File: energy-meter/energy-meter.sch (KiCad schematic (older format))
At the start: 28 parts, among them J1 Screw_Terminal_01x04, J2 Conn_01x03, K1 G5RL-U1A-E, P1 PineNut, T1 AP-2500, T2 BV 202 0154, U1 L9110S, U9 GD32VF103

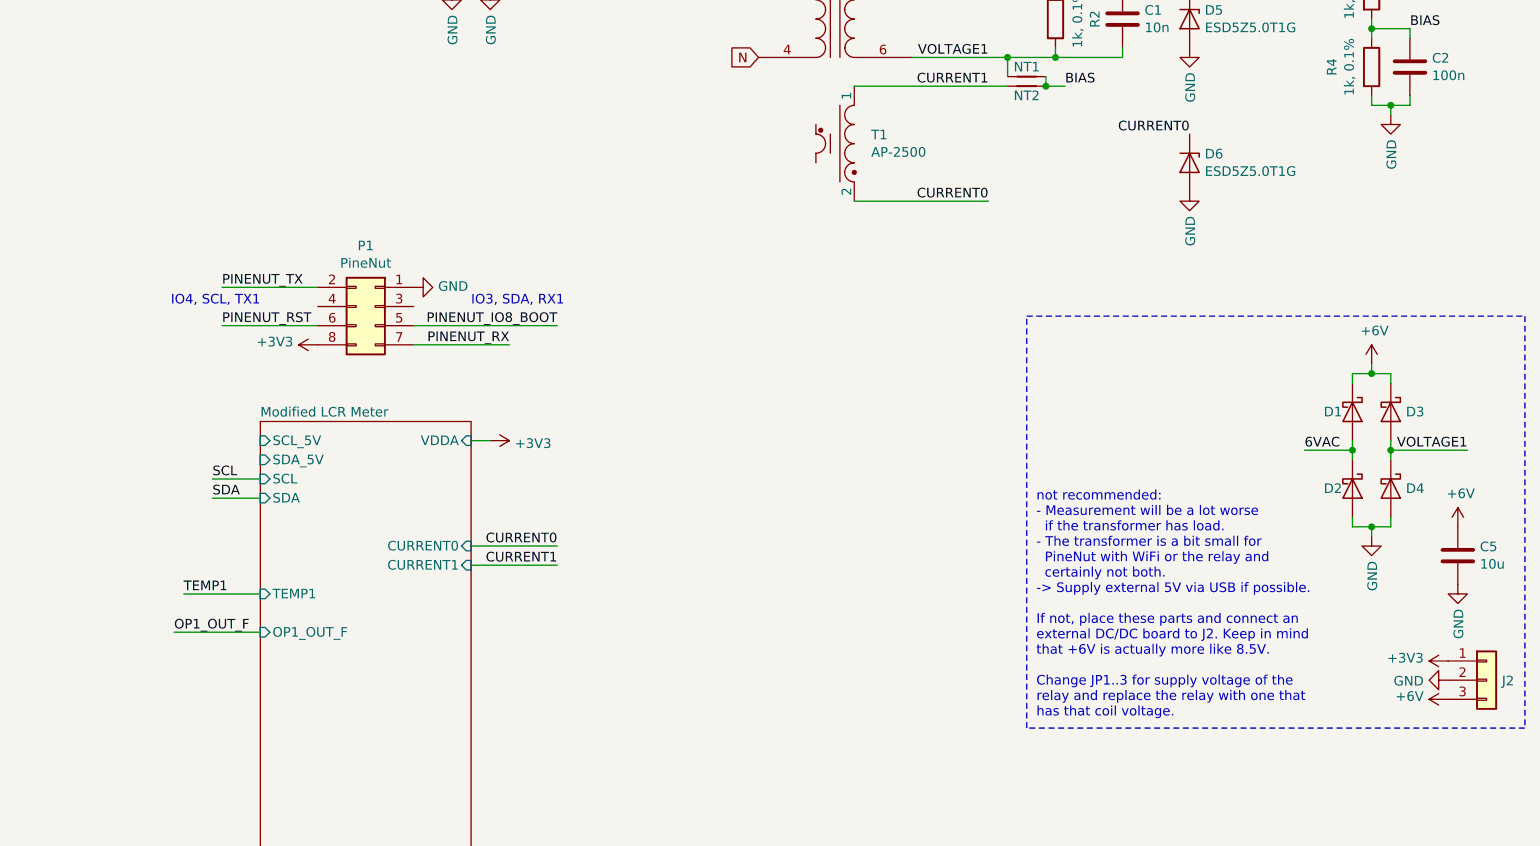
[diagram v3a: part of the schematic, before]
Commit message: DRC, add header for I2C
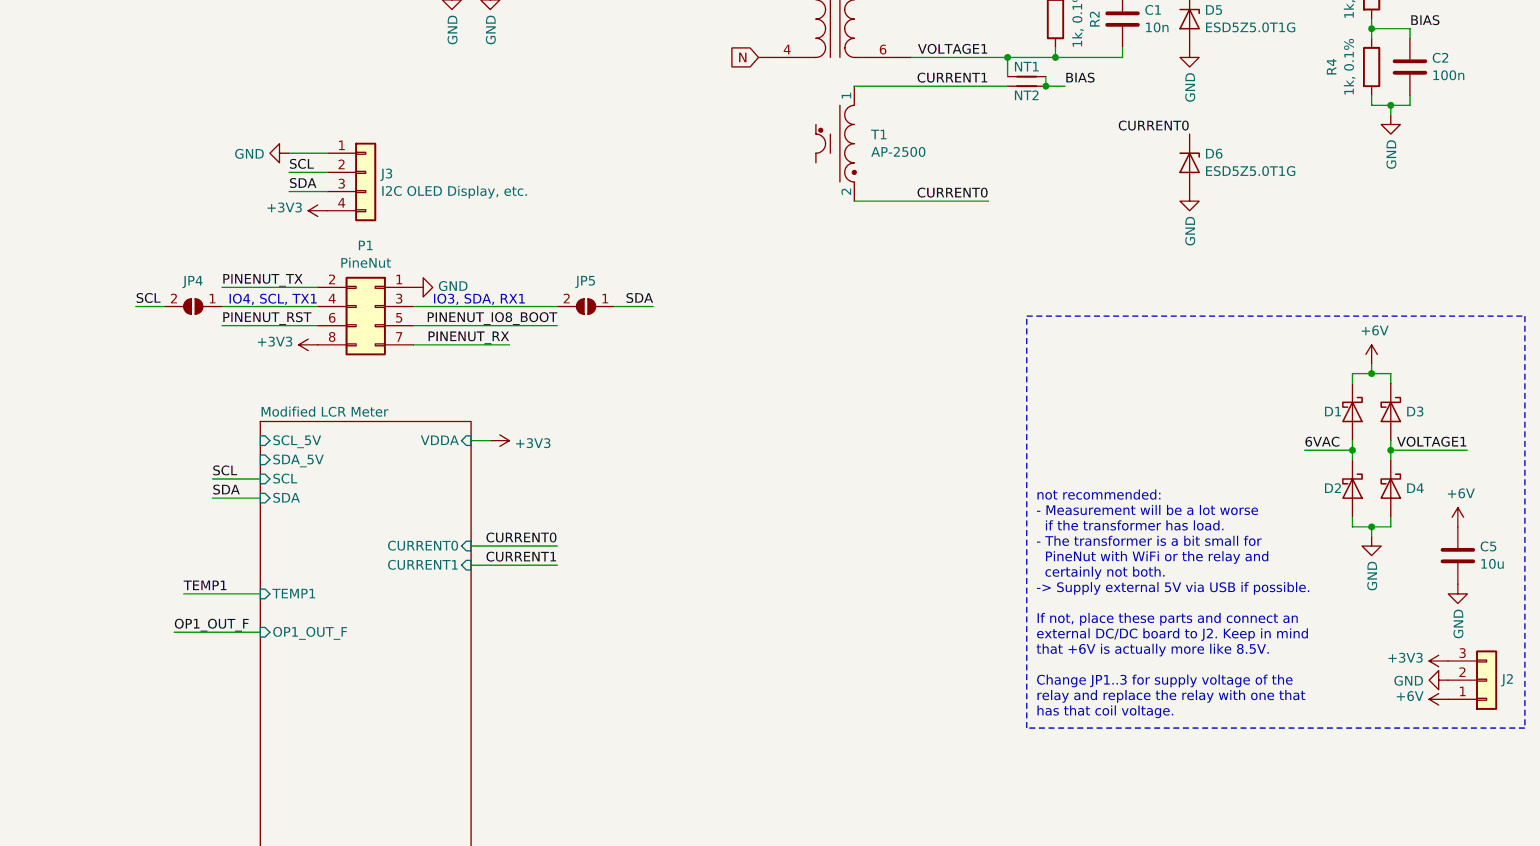
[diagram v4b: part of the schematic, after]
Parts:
- added J3: I2C OLED Display, etc., Connector_PinHeader_2.54mm:PinHeader_1x04_P2.54mm_Horizontal, symbol Connector_Generic:Conn_01x04
- added JP4, JP5: SolderJumper_2_Open, Jumper:SolderJumper-2_P1.3mm_Open_RoundedPad1.0x1.5mm, symbol Jumper:SolderJumper_2_Open
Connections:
- net +3V3: now also J2.3 (Pin_3), J3.4 (Pin_4); no longer J2.1 (Pin_1)
- net +6V: now also J2.1 (Pin_1); no longer J2.3 (Pin_3)
- net GND: now also J3.1 (Pin_1)
- net SCL: now also J3.2 (Pin_2), JP4.2 (B)
- net SDA: now also J3.3 (Pin_3), JP5.1 (A)
- net at P1.3 (Pin_3): now also JP5.2 (B)
- net at P1.4 (Pin_4): now also JP4.1 (A)
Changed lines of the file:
@@
 	0    -1   -1   0
 $EndComp
-Text Notes 5600 4250 0    50   ~ 0
+Text Notes 5400 4250 0    50   ~ 0
 IO3, SDA, RX1
-Text Notes 4500 4250 2    50   ~ 0
+Text Notes 4800 4250 2    50   ~ 0
 IO4, SCL, TX1
 $Comp
@@
 F 3 "~" H 10900 6200 50  0001 C CNN
 	1    10900 6200
-	1    0    0    -1
+	1    0    0    1
 $EndComp
 $Comp
@@
 Text Label 9350 3350 2    50   ~ 0
 CURRENT0
+Text Label 3850 4250 0    50   ~ 0
+SCL
+Wire Wire Line
+	4300 4250 4800 4250
+$Comp
+L Jumper:SolderJumper_2_Open JP4
+U 1 1 60C77BF5
+P 4150 4250
+F 0 "JP4" H 4150 4117 50  0000 C CNN
+F 1 "SolderJumper_2_Open" H 4150 4364 50  0001 C CNN
+F 2 "Jumper:SolderJumper-2_P1.3mm_Open_RoundedPad1.0x1.5mm" H 4150 4250 50  0001 C CNN
+F 3 "~" H 4150 4250 50  0001 C CNN
+	1    4150 4250
+	-1   0    0    1
+$EndComp
+Wire Wire Line
+	3850 4250 4000 4250
+Wire Wire Line
+	5300 4250 6050 4250
+$Comp
+L Jumper:SolderJumper_2_Open JP5
+U 1 1 60C8116D
+P 6200 4250
+F 0 "JP5" H 6200 4117 50  0000 C CNN
+F 1 "SolderJumper_2_Open" H 6200 4364 50  0001 C CNN
+F 2 "Jumper:SolderJumper-2_P1.3mm_Open_RoundedPad1.0x1.5mm" H 6200 4250 50  0001 C CNN
+F 3 "~" H 6200 4250 50  0001 C CNN
+	1    6200 4250
+	-1   0    0    1
+$EndComp
+Text Label 6550 4250 2    50   ~ 0
+SDA
+Wire Wire Line
+	6550 4250 6350 4250
+$Comp
+L Connector_Generic:Conn_01x04 J3
+U 1 1 60C9802A
+P 5050 3550
+F 0 "J3" H 5130 3542 50  0000 L CNN
+F 1 "I2C OLED Display, etc." H 5130 3451 50  0000 L CNN
+F 2 "Connector_PinHeader_2.54mm:PinHeader_1x04_P2.54mm_Horizontal" H 5050 3550 50  0001 C CNN
+F 3 "~" H 5050 3550 50  0001 C CNN
+	1    5050 3550
+	1    0    0    -1
+$EndComp
+$Comp
+L power:GND #PWR0136
+U 1 1 60C999E8
+P 4650 3450
+F 0 "#PWR0136" H 4650 3200 50  0001 C CNN
+F 1 "GND" V 4655 3322 50  0000 R CNN
+F 2 "" H 4650 3450 50  0001 C CNN
+F 3 "" H 4650 3450 50  0001 C CNN
+	1    4650 3450
+	0    1    1    0
+$EndComp
+Text Label 4650 3550 0    50   ~ 0
+SCL
+Wire Wire Line
+	4650 3550 4850 3550
+Text Label 4650 3650 0    50   ~ 0
+SDA
+Wire Wire Line
+	4650 3650 4850 3650
+$Comp
+L power:+3V3 #PWR?
+U 1 1 60CA251B
+P 4850 3750
+AR Path="/607B74C2/60CA251B" Ref="#PWR?"  Part="1"
+AR Path="/60CA251B" Ref="#PWR0137"  Part="1"
+F 0 "#PWR0137" H 4850 3600 50  0001 C CNN
+F 1 "+3V3" V 4865 3878 50  0000 L CNN
+F 2 "" H 4850 3750 50  0001 C CNN
+F 3 "" H 4850 3750 50  0001 C CNN
+	1    4850 3750
+	0    -1   -1   0
+$EndComp
+Wire Wire Line
+	4650 3450 4850 3450
 $EndSCHEMATC

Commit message: add alternative relay
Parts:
- added K2: DNP / HF3FF/005-1HST, energy-meter:Relay_HF3FF_005, symbol Relay:DIPxx-1Axx-11x
- added T3: DNP / AP-2500, energy-meter:AP-2500, symbol energy-meter:AP-2500
- added TP?: TestPoint, TestPoint:TestPoint_THTPad_D3.0mm_Drill1.5mm, symbol Connector:TestPoint
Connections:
- net labels added: coil+, coil-
- wire segments 114 -> 125
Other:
- note added: "alternative relay:\ncheap but not bistable"
- note added: "connect with wire"
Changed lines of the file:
@@
 Wire Wire Line
 	4650 3450 4850 3450
+$Comp
+L Relay:DIPxx-1Axx-11x K2
+U 1 1 60CDDACF
+P 9700 1200
+F 0 "K2" H 10030 1246 50  0000 L CNN
+F 1 "DNP / HF3FF/005-1HST" H 10030 1155 50  0000 L CNN
+F 2 "energy-meter:Relay_HF3FF_005" H 10050 1150 50  0001 L CNN
+F 3 "https://standexelectronics.com/wp-content/uploads/datasheet_reed_relay_DIP.pdf" H 9700 1200 50  0001 C CNN
+F 4 "https://www.tme.eu/de/details/hf3ff_005-1hst/elektromagnetische-mini-relais/hongfa-relay/" H 9700 1200 50  0001 C CNN "TME"
+	1    9700 1200
+	1    0    0    -1
+$EndComp
+Text GLabel 9950 850  2    50   Input ~ 0
+L_OUT
+Wire Wire Line
+	9950 850  9900 850
+Wire Wire Line
+	9900 850  9900 900
+Text GLabel 10350 1550 2    50   Input ~ 0
+L_IN
+Wire Wire Line
+	9900 1550 9900 1500
+Text Notes 9550 750  0    50   ~ 0
+alternative relay:\ncheap but not bistable
+Text Label 6850 2200 0    50   ~ 0
+coil+
+Text Label 6850 1500 0    50   ~ 0
+coil-
+Text Label 9100 850  0    50   ~ 0
+coil-
+Text Label 9100 1550 0    50   ~ 0
+coil+
+Wire Wire Line
+	9100 1550 9500 1550
+Wire Wire Line
+	9500 1550 9500 1500
+Wire Wire Line
+	9100 850  9500 850
+Wire Wire Line
+	9500 850  9500 900
+Text Notes 10050 1700 0    50   ~ 0
+connect with wire
+$Comp
+L energy-meter:AP-2500 T3
+U 1 1 60CFE5A9
+P 7100 3400
+F 0 "T3" V 7050 3250 50  0000 L CNN
+F 1 "DNP / AP-2500" V 7150 2750 50  0000 L CNN
+F 2 "energy-meter:AP-2500" H 7100 3400 50  0001 C CNN
+F 3 "https://www.coilcraft.com/pdfs/cst.pdf" H 7100 3400 50  0001 C CNN
+F 4 "https://www.tme.eu/de/details/ap-2500/stromwandler/talema/" V 7100 3400 50  0001 C CNN "TME"
+	1    7100 3400
+	0    1    1    0
+$EndComp
+Wire Wire Line
+	7300 3100 7600 3100
+Connection ~ 7600 3100
+Wire Wire Line
+	7600 3700 7300 3700
+Connection ~ 7600 3700
+$Comp
+L Connector:TestPoint TP?
+U 1 1 60D46B3F
+P 9900 1550
+F 0 "TP?" H 9950 1800 50  0000 R CNN
+F 1 "TestPoint" H 9958 1577 50  0001 L CNN
+F 2 "TestPoint:TestPoint_THTPad_D3.0mm_Drill1.5mm" H 10100 1550 50  0001 C CNN
+F 3 "~" H 10100 1550 50  0001 C CNN
+	1    9900 1550
+	-1   0    0    1
+$EndComp
+Connection ~ 9900 1550
+Wire Wire Line
+	10350 1550 10200 1550
+Wire Wire Line
+	9900 1550 10100 1550
 $EndSCHEMATC

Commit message: add optional internal load resistor
This may be useful for calibration and tests.
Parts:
- added R5: 39kOhm, 2W, 1%, Resistor_SMD:R_2512_6332Metric_Pad1.52x3.35mm_HandSolder, symbol Device:R
- added TP2, TP3, TP4, TP5: TestPoint, TestPoint:TestPoint_THTPad_D3.0mm_Drill1.5mm, symbol Connector:TestPoint
- gave numbers to parts that had none: 1
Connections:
- wire segments 125 -> 133
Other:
- note added: "alternative use of the 2nd relay:\n- cut L_OUT around TP3\n- TP3 -> through T3 -> TP5\n- N -> TP4\n- L_OUT to external load, as usual\n=> K2 enables internal load"
- moved on the sheet: C2, R3, R4, TP1
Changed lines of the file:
@@
 P 7750 900
 F 0 "J1" H 7830 892 50  0000 L CNN
-F 1 "Screw_Terminal_01x04" H 7830 801 50  0000 L CNN
+F 1 "Screw_Terminal_01x04" H 7830 801 50  0001 L CNN
 F 2 "energy-meter:DG35C-B-04P-13-200AH" H 7750 900 50  0001 C CNN
 F 3 "~" H 7750 900 50  0001 C CNN
@@
 U 1 1 60929B00
 P 7500 2750
-F 0 "T2" H 7500 3131 50  0000 C CNN
+F 0 "T2" H 7300 2750 50  0000 C CNN
 F 1 "BV 202 0154" H 7500 3040 50  0000 C CNN
 F 2 "energy-meter:BV202" H 7500 2750 50  0001 C CNN
@@
 Wire Wire Line
 	6050 5600 5600 5600
-Text Label 8700 2550 0    50   ~ 0
+Text Label 9050 2550 0    50   ~ 0
 VOLTAGE0
 Text Label 8300 2950 2    50   ~ 0
@@
 L Device:R R?
 U 1 1 60A38A5B
-P 10300 3000
+P 10500 3300
 AR Path="/602A3FC4/60A38A5B" Ref="R?"  Part="1"
 AR Path="/60514CC5/60A38A5B" Ref="R?"  Part="1"
 AR Path="/607B74C2/60A38A5B" Ref="R?"  Part="1"
 AR Path="/60A38A5B" Ref="R4"  Part="1"
-F 0 "R4" V 10093 3000 50  0000 C CNN
-F 1 "1k, 0.1%" V 10184 3000 50  0000 C CNN
-F 2 "Resistor_SMD:R_0603_1608Metric_Pad1.05x0.95mm_HandSolder" V 10230 3000 50  0001 C CNN
-F 3 "~" H 10300 3000 50  0001 C CNN
-	1    10300 3000
+F 0 "R4" V 10293 3300 50  0000 C CNN
+F 1 "1k, 0.1%" V 10384 3300 50  0000 C CNN
+F 2 "Resistor_SMD:R_0603_1608Metric_Pad1.05x0.95mm_HandSolder" V 10430 3300 50  0001 C CNN
+F 3 "~" H 10500 3300 50  0001 C CNN
+	1    10500 3300
 	1    0    0    -1
 $EndComp
@@
 L Device:C C?
 U 1 1 60A38A61
-P 10500 3000
+P 10700 3300
 AR Path="/602A2F7F/60A38A61" Ref="C?"  Part="1"
 AR Path="/602A3FC4/60A38A61" Ref="C?"  Part="1"
@@
 AR Path="/607B74C2/60A38A61" Ref="C?"  Part="1"
 AR Path="/60A38A61" Ref="C2"  Part="1"
-F 0 "C2" H 10615 3046 50  0000 L CNN
-F 1 "100n" H 10615 2955 50  0000 L CNN
-F 2 "Capacitor_SMD:C_0603_1608Metric_Pad1.05x0.95mm_HandSolder" H 10538 2850 50  0001 C CNN
-F 3 "~" H 10500 3000 50  0001 C CNN
-	1    10500 3000
+F 0 "C2" H 10815 3346 50  0000 L CNN
+F 1 "100n" H 10815 3255 50  0000 L CNN
+F 2 "Capacitor_SMD:C_0603_1608Metric_Pad1.05x0.95mm_HandSolder" H 10738 3150 50  0001 C CNN
+F 3 "~" H 10700 3300 50  0001 C CNN
+	1    10700 3300
 	1    0    0    -1
 $EndComp
@@
 L power:+3V3 #PWR?
 U 1 1 60A3967A
-P 10300 2400
+P 10500 2700
 AR Path="/607B74C2/60A3967A" Ref="#PWR?"  Part="1"
 AR Path="/60A3967A" Ref="#PWR0106"  Part="1"
-F 0 "#PWR0106" H 10300 2250 50  0001 C CNN
-F 1 "+3V3" V 10315 2528 50  0000 L CNN
-F 2 "" H 10300 2400 50  0001 C CNN
-F 3 "" H 10300 2400 50  0001 C CNN
-	1    10300 2400
+F 0 "#PWR0106" H 10500 2550 50  0001 C CNN
+F 1 "+3V3" V 10515 2828 50  0000 L CNN
+F 2 "" H 10500 2700 50  0001 C CNN
+F 3 "" H 10500 2700 50  0001 C CNN
+	1    10500 2700
 	1    0    0    -1
 $EndComp
@@
 L Device:R R?
 U 1 1 60A3A4C3
-P 10300 2600
+P 10500 2900
 AR Path="/602A3FC4/60A3A4C3" Ref="R?"  Part="1"
 AR Path="/60514CC5/60A3A4C3" Ref="R?"  Part="1"
 AR Path="/607B74C2/60A3A4C3" Ref="R?"  Part="1"
 AR Path="/60A3A4C3" Ref="R3"  Part="1"
-F 0 "R3" V 10093 2600 50  0000 C CNN
-F 1 "1k, 0.1%" V 10184 2600 50  0000 C CNN
-F 2 "Resistor_SMD:R_0603_1608Metric_Pad1.05x0.95mm_HandSolder" V 10230 2600 50  0001 C CNN
-F 3 "~" H 10300 2600 50  0001 C CNN
-	1    10300 2600
-	1    0    0    -1
-$EndComp
-Wire Wire Line
-	10500 3150 10500 3200
-Wire Wire Line
-	10500 3200 10400 3200
-Wire Wire Line
-	10400 3200 10400 3250
-Wire Wire Line
-	10400 3200 10300 3200
-Wire Wire Line
-	10300 3200 10300 3150
-Connection ~ 10400 3200
-Wire Wire Line
-	10300 2850 10300 2800
-Wire Wire Line
-	10300 2800 10500 2800
-Wire Wire Line
-	10500 2800 10500 2850
-Connection ~ 10300 2800
-Wire Wire Line
-	10300 2800 10300 2750
-Wire Wire Line
-	10300 2450 10300 2400
+F 0 "R3" V 10293 2900 50  0000 C CNN
+F 1 "1k, 0.1%" V 10384 2900 50  0000 C CNN
+F 2 "Resistor_SMD:R_0603_1608Metric_Pad1.05x0.95mm_HandSolder" V 10430 2900 50  0001 C CNN
+F 3 "~" H 10500 2900 50  0001 C CNN
+	1    10500 2900
+	1    0    0    -1
+$EndComp
+Wire Wire Line
+	10700 3450 10700 3500
+Wire Wire Line
+	10700 3500 10600 3500
+Wire Wire Line
+	10600 3500 10600 3550
+Wire Wire Line
+	10600 3500 10500 3500
+Wire Wire Line
+	10500 3500 10500 3450
+Connection ~ 10600 3500
+Wire Wire Line
+	10500 3150 10500 3100
+Wire Wire Line
+	10500 3100 10700 3100
+Wire Wire Line
+	10700 3100 10700 3150
+Connection ~ 10500 3100
+Wire Wire Line
+	10500 3100 10500 3050
+Wire Wire Line
+	10500 2750 10500 2700
 $Comp
 L power:GND #PWR0107
 U 1 1 60A40FDE
-P 10400 3250
-F 0 "#PWR0107" H 10400 3000 50  0001 C CNN
-F 1 "GND" V 10405 3122 50  0000 R CNN
-F 2 "" H 10400 3250 50  0001 C CNN
-F 3 "" H 10400 3250 50  0001 C CNN
-	1    10400 3250
-	1    0    0    -1
-$EndComp
-Text Label 10500 2800 0    50   ~ 0
+P 10600 3550
+F 0 "#PWR0107" H 10600 3300 50  0001 C CNN
+F 1 "GND" V 10605 3422 50  0000 R CNN
+F 2 "" H 10600 3550 50  0001 C CNN
+F 3 "" H 10600 3550 50  0001 C CNN
+	1    10600 3550
+	1    0    0    -1
+$EndComp
+Text Label 10700 3100 0    50   ~ 0
 BIAS
 $Comp
@@
 U 1 1 60CDDACF
 P 9700 1200
-F 0 "K2" H 10030 1246 50  0000 L CNN
-F 1 "DNP / HF3FF/005-1HST" H 10030 1155 50  0000 L CNN
+F 0 "K2" H 10050 1350 50  0000 L CNN
+F 1 "DNP / HF3FF/005-1HST" H 10050 1250 50  0000 L CNN
 F 2 "energy-meter:Relay_HF3FF_005" H 10050 1150 50  0001 L CNN
 F 3 "https://standexelectronics.com/wp-content/uploads/datasheet_reed_relay_DIP.pdf" H 9700 1200 50  0001 C CNN
@@
 Wire Wire Line
 	9900 850  9900 900
-Text GLabel 10350 1550 2    50   Input ~ 0
+Text GLabel 10400 1550 2    50   Input ~ 0
 L_IN
 Wire Wire Line
@@
 Wire Wire Line
 	9500 850  9500 900
-Text Notes 10050 1700 0    50   ~ 0
+Text Notes 10350 1750 0    50   ~ 0
 connect with wire
 $Comp
@@
 Connection ~ 7600 3700
 $Comp
-L Connector:TestPoint TP?
+L Connector:TestPoint TP1
 U 1 1 60D46B3F
-P 9900 1550
-F 0 "TP?" H 9950 1800 50  0000 R CNN
-F 1 "TestPoint" H 9958 1577 50  0001 L CNN
-F 2 "TestPoint:TestPoint_THTPad_D3.0mm_Drill1.5mm" H 10100 1550 50  0001 C CNN
-F 3 "~" H 10100 1550 50  0001 C CNN
-	1    9900 1550
+P 10100 1550
+F 0 "TP1" H 10150 1800 50  0000 R CNN
+F 1 "TestPoint" H 10158 1577 50  0001 L CNN
+F 2 "TestPoint:TestPoint_THTPad_D3.0mm_Drill1.5mm" H 10300 1550 50  0001 C CNN
+F 3 "~" H 10300 1550 50  0001 C CNN
+	1    10100 1550
 	-1   0    0    1
 $EndComp
-Connection ~ 9900 1550
-Wire Wire Line
-	10350 1550 10200 1550
+Wire Wire Line
+	10400 1550 10250 1550
 Wire Wire Line
 	9900 1550 10100 1550
+$Comp
+L Connector:TestPoint TP2
+U 1 1 60D5530D
+P 10250 1550
+F 0 "TP2" H 10300 1800 50  0000 R CNN
+F 1 "TestPoint" H 10308 1577 50  0001 L CNN
+F 2 "TestPoint:TestPoint_THTPad_D3.0mm_Drill1.5mm" H 10450 1550 50  0001 C CNN
+F 3 "~" H 10450 1550 50  0001 C CNN
+	1    10250 1550
+	-1   0    0    1
+$EndComp
+$Comp
+L Connector:TestPoint TP3
+U 1 1 60D6E7AC
+P 10750 750
+F 0 "TP3" H 10800 1000 50  0000 R CNN
+F 1 "TestPoint" H 10808 777 50  0001 L CNN
+F 2 "TestPoint:TestPoint_THTPad_D3.0mm_Drill1.5mm" H 10950 750 50  0001 C CNN
+F 3 "~" H 10950 750 50  0001 C CNN
+	1    10750 750
+	0    -1   -1   0
+$EndComp
+Text Notes 8650 2050 0    50   ~ 0
+alternative use of the 2nd relay:\n- cut L_OUT around TP3\n- TP3 -> through T3 -> TP5\n- N -> TP4\n- L_OUT to external load, as usual\n=> K2 enables internal load
+$Comp
+L Connector:TestPoint TP4
+U 1 1 60D74A76
+P 10850 1400
+F 0 "TP4" H 10900 1650 50  0000 R CNN
+F 1 "TestPoint" H 10908 1427 50  0001 L CNN
+F 2 "TestPoint:TestPoint_THTPad_D3.0mm_Drill1.5mm" H 11050 1400 50  0001 C CNN
+F 3 "~" H 11050 1400 50  0001 C CNN
+	1    10850 1400
+	0    1    1    0
+$EndComp
+Wire Notes Line
+	8600 2100 11150 2100
+Wire Notes Line
+	11150 2100 11150 600
+Wire Notes Line
+	11150 600  8600 600
+Wire Notes Line
+	8600 600  8600 2100
+$Comp
+L Device:R R5
+U 1 1 60D8261D
+P 10500 1400
+F 0 "R5" V 10400 1300 50  0000 C CNN
+F 1 "39kOhm, 2W, 1%" V 10350 1700 50  0000 C CNN
+F 2 "Resistor_SMD:R_2512_6332Metric_Pad1.52x3.35mm_HandSolder" V 10430 1400 50  0001 C CNN
+F 3 "~" H 10500 1400 50  0001 C CNN
+F 4 "https://www.tme.eu/de/details/sp12-39k-1%25/widerstande-smd-2512/royal-ohm/sp123wf3902t2e/" H 10500 1400 50  0001 C CNN "TME"
+	1    10500 1400
+	0    1    1    0
+$EndComp
+Wire Wire Line
+	10650 1400 10850 1400
+Wire Wire Line
+	10350 1400 10100 1400
+Wire Wire Line
+	10100 1400 10100 1550
+Connection ~ 10100 1550
+$Comp
+L Connector:TestPoint TP5
+U 1 1 60D9EED0
+P 10750 950
+F 0 "TP5" H 10800 1200 50  0000 R CNN
+F 1 "TestPoint" H 10808 977 50  0001 L CNN
+F 2 "TestPoint:TestPoint_THTPad_D3.0mm_Drill1.5mm" H 10950 950 50  0001 C CNN
+F 3 "~" H 10950 950 50  0001 C CNN
+	1    10750 950
+	0    -1   -1   0
+$EndComp
+Text GLabel 10850 850  2    50   Input ~ 0
+L_OUT
+Wire Wire Line
+	10850 850  10800 850
+Wire Wire Line
+	10800 850  10800 750
+Wire Wire Line
+	10800 750  10750 750
+Wire Wire Line
+	10800 850  10800 950
+Wire Wire Line
+	10800 950  10750 950
+Connection ~ 10800 850
 $EndSCHEMATC

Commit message: 2nd relay needs an additional driver if we want to use both of them
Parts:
- added D7: D_Schottky, Diode_SMD:D_SMA_Handsoldering, symbol Device:D_Schottky
- added Q1: AP3400, Package_TO_SOT_SMD:SOT-23_Handsoldering, symbol Device:Q_NMOS_GSD
- added R? (x3): 10k, Resistor_SMD:R_0603_1608Metric_Pad1.05x0.95mm_HandSolder, symbol Device:R
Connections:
- net labels added: RELAY2, VCC_COIL
- wire segments 133 -> 148
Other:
- moved on the sheet: C1, C2, C3, C4, D5, D6, J1, J3, JP1, JP2, JP3, JP4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

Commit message: adjust voltage divider to somewhat work if transformer is also used for VCC
In that case, we will only see one half of the wave.
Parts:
- removed NT1: Net-Tie_2, NetTie:NetTie-2_SMD_Pad0.5mm, symbol Device:Net-Tie_2
- added D8, D9: ESD5Z5.0T1G, Diode_SMD:D_SOD-523, symbol Device:D_Zener
- added JP6, JP7: SolderJumper_2_Bridged, Jumper:SolderJumper-2_P1.3mm_Bridged_RoundedPad1.0x1.5mm, symbol Jumper:SolderJumper_2_Bridged
- added JP8: SolderJumper_2_Open, Jumper:SolderJumper-2_P1.3mm_Open_RoundedPad1.0x1.5mm, symbol Jumper:SolderJumper_2_Open
- gave numbers to parts that had none: 3
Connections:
- net labels added: VOLTAGE1B
- wire segments 148 -> 149
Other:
- moved on the sheet: C2, C5, D1, D2, D3, D4, J2, NT2, R3, R4, T1, T3
